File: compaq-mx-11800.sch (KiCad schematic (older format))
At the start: 238 parts

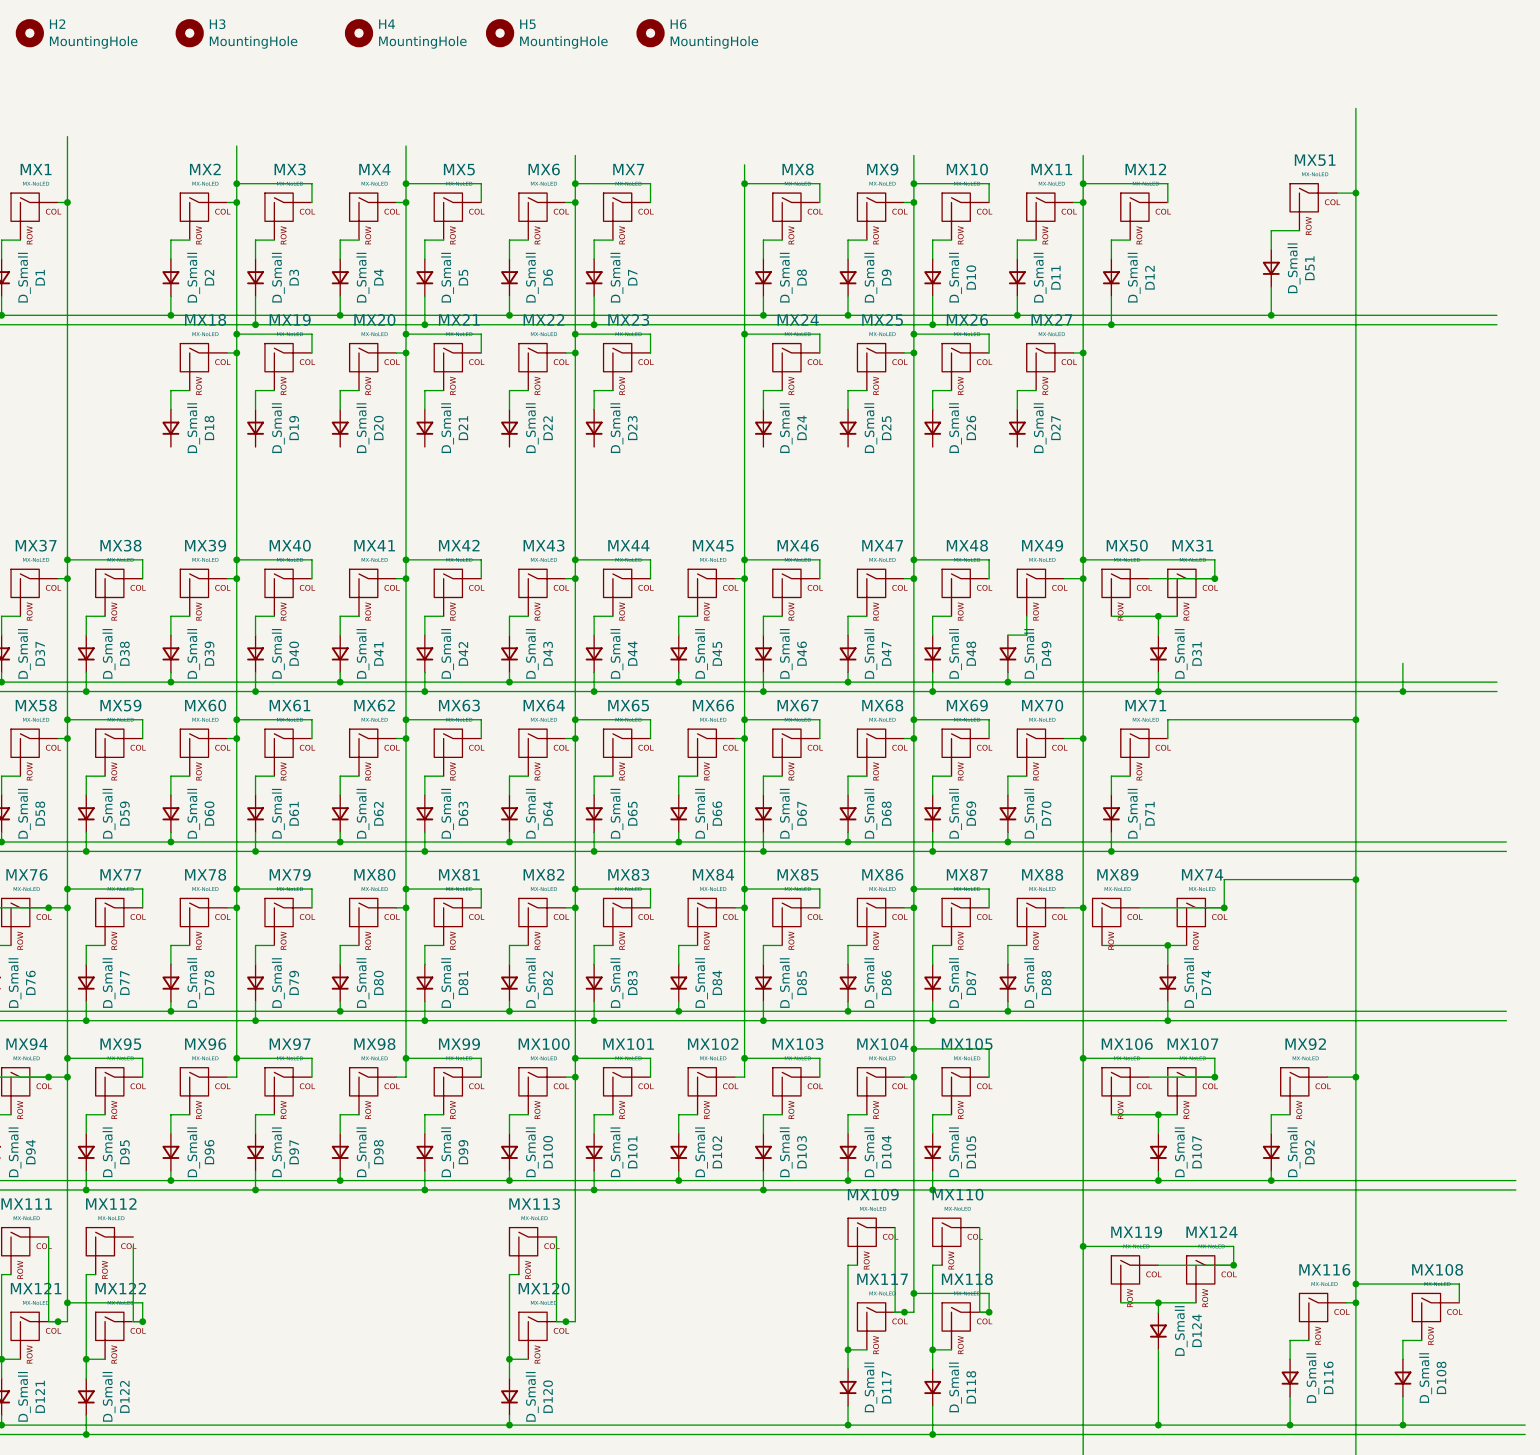
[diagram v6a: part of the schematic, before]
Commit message: fix multilayout column pin connections
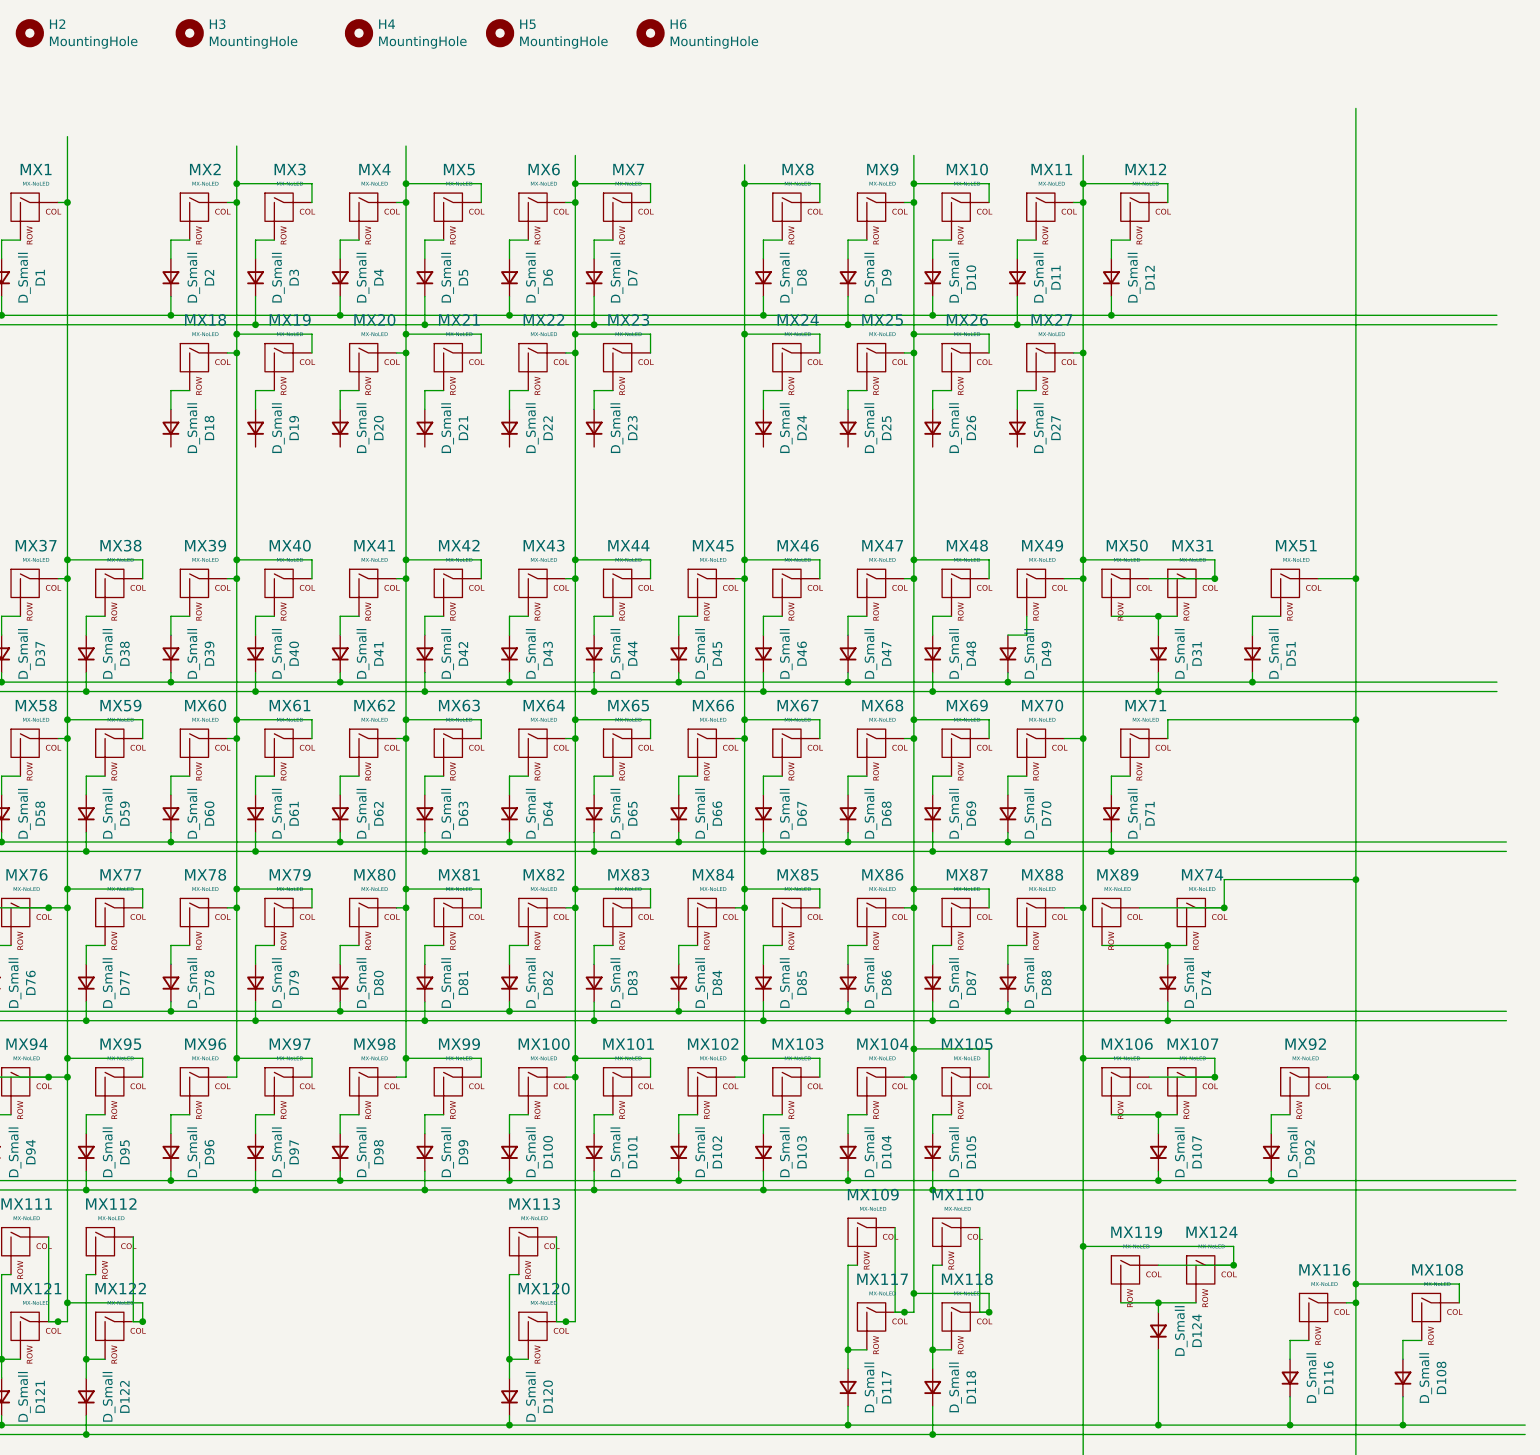
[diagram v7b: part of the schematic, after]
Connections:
- wire segments 748 -> 746
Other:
- moved on the sheet: D51, MX51
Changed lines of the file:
@@
 Wire Wire Line
 	8200 10600 8900 10600
-Wire Wire Line
-	14800 8700 16850 8700
-Connection ~ 14800 8700
-Wire Wire Line
-	14800 8550 14800 8700
-Wire Wire Line
-	14300 8650 15650 8650
-Connection ~ 14300 8650
-Wire Wire Line
-	14300 8550 14300 8650
-Wire Wire Line
-	13400 8650 14300 8650
-Wire Wire Line
-	13850 8700 14800 8700
-Connection ~ 13850 8700
-Wire Wire Line
-	13850 8550 13850 8700
-Connection ~ 13400 8650
-Wire Wire Line
-	13400 8550 13400 8650
-Wire Wire Line
-	12050 8700 13850 8700
-Wire Wire Line
-	12950 8650 13400 8650
 Connection ~ 12950 8650
 Wire Wire Line
-	15650 8650 16850 8650
-Connection ~ 15650 8650
-Wire Wire Line
-	15650 8500 15650 8650
-Wire Wire Line
 	12950 8550 12950 8650
 Connection ~ 12050 8700
@@
 L Device:D_Small D51
 U 1 1 61E61DC5
-P 15650 8400
-F 0 "D51" H 15650 8193 50  0000 C CNN
-F 1 "D_Small" H 15650 8284 50  0000 C CNN
-F 2 "Keebio-Parts:Diode-dual" V 15650 8400 50  0001 C CNN
-F 3 "~" V 15650 8400 50  0001 C CNN
-	1    15650 8400
+P 15550 10450
+F 0 "D51" H 15550 10243 50  0000 C CNN
+F 1 "D_Small" H 15550 10334 50  0000 C CNN
+F 2 "Keebio-Parts:Diode-dual" V 15550 10450 50  0001 C CNN
+F 3 "~" V 15550 10450 50  0001 C CNN
+	1    15550 10450
 	0    -1   -1   0
 $EndComp
@@
 L MX_Alps_Hybrid:MX-NoLED MX51
 U 1 1 61E61DCB
-P 15850 8050
-F 0 "MX51" H 15883 8273 60  0000 C CNN
-F 1 "MX-NoLED" H 15883 8199 20  0000 C CNN
-F 2 "MX_Only:MXOnly-1U-NoLED" H 15225 8025 60  0001 C CNN
-F 3 "" H 15225 8025 60  0001 C CNN
-	1    15850 8050
+P 15750 10100
+F 0 "MX51" H 15783 10323 60  0000 C CNN
+F 1 "MX-NoLED" H 15783 10249 20  0000 C CNN
+F 2 "MX_Only:MXOnly-1U-NoLED" H 15125 10075 60  0001 C CNN
+F 3 "" H 15125 10075 60  0001 C CNN
+	1    15750 10100
 	1    0    0    -1
 $EndComp
 Wire Wire Line
-	15800 8200 15650 8200
-Wire Wire Line
-	15650 8200 15650 8300
-Wire Wire Line
-	16000 8000 16100 8000
-Connection ~ 16100 8000
+	15700 10250 15550 10250
 Wire Wire Line
-	16100 7550 16100 8000
+	15550 10250 15550 10350
 $Comp
 L MX_Alps_Hybrid:MX-NoLED MX1
@@
 Connection ~ 15650 13250
 Wire Wire Line
-	14250 10600 16850 10600
+	14250 10600 15550 10600
 Connection ~ 14650 13600
 Wire Wire Line
@@
 	10050 17250 10050 17350
 Wire Wire Line
-	16350 10650 16850 10650
-Wire Wire Line
-	15050 10650 16350 10650
-Connection ~ 16350 10650
-Wire Wire Line
-	16350 10500 16350 10650
-Wire Wire Line
 	16350 14100 16350 14200
 Wire Wire Line
@@
 Connection ~ 16100 13800
 Wire Wire Line
-	16100 8000 16100 10800
-Wire Wire Line
 	16350 14400 16350 14550
 Wire Wire Line
@@
 Connection ~ 11900 14000
 Wire Wire Line
-	9600 13600 9600 14000
-Wire Wire Line
 	9600 14000 9650 14000
 Connection ~ 9650 14000
@@
 	9150 14000 9200 14000
 Connection ~ 9200 14000
+Wire Wire Line
+	12050 8700 13400 8700
+Wire Wire Line
+	12950 8650 13850 8650
+Wire Wire Line
+	13400 8550 13400 8700
+Connection ~ 13400 8700
+Wire Wire Line
+	13850 8550 13850 8650
+Connection ~ 13850 8650
+Wire Wire Line
+	13850 8650 14800 8650
+Wire Wire Line
+	14300 8550 14300 8700
+Wire Wire Line
+	13400 8700 14300 8700
+Connection ~ 14300 8700
+Wire Wire Line
+	14800 8550 14800 8650
+Connection ~ 14800 8650
+Wire Wire Line
+	14800 8650 16850 8650
+Wire Wire Line
+	16100 7550 16100 10050
+Wire Wire Line
+	15550 10550 15550 10600
+Connection ~ 15550 10600
+Wire Wire Line
+	15550 10600 16850 10600
+Wire Wire Line
+	15900 10050 16100 10050
+Connection ~ 16100 10050
+Wire Wire Line
+	16100 10050 16100 10800
+Wire Wire Line
+	15050 10650 16850 10650
+Wire Wire Line
+	14300 8700 16850 8700
+Wire Wire Line
+	9600 13550 9600 14000
 $EndSCHEMATC

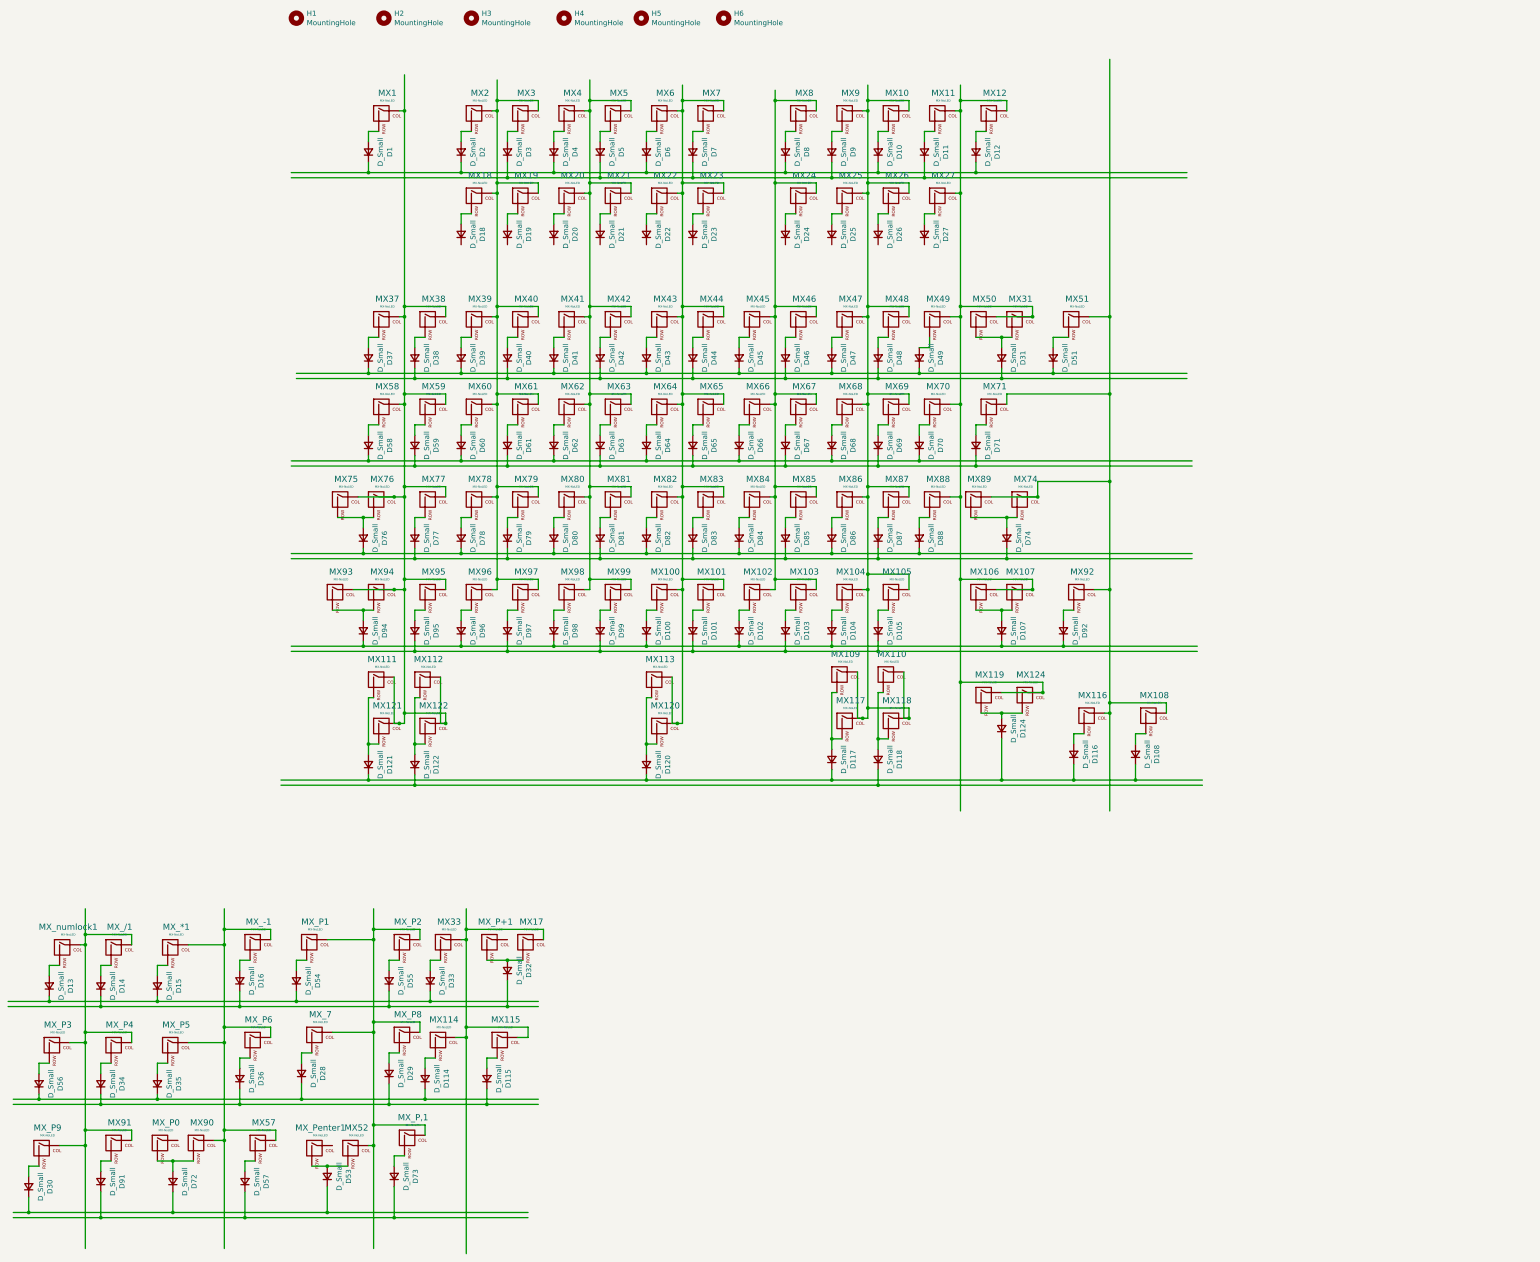
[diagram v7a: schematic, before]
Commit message: connect numpad to existing rows and columns
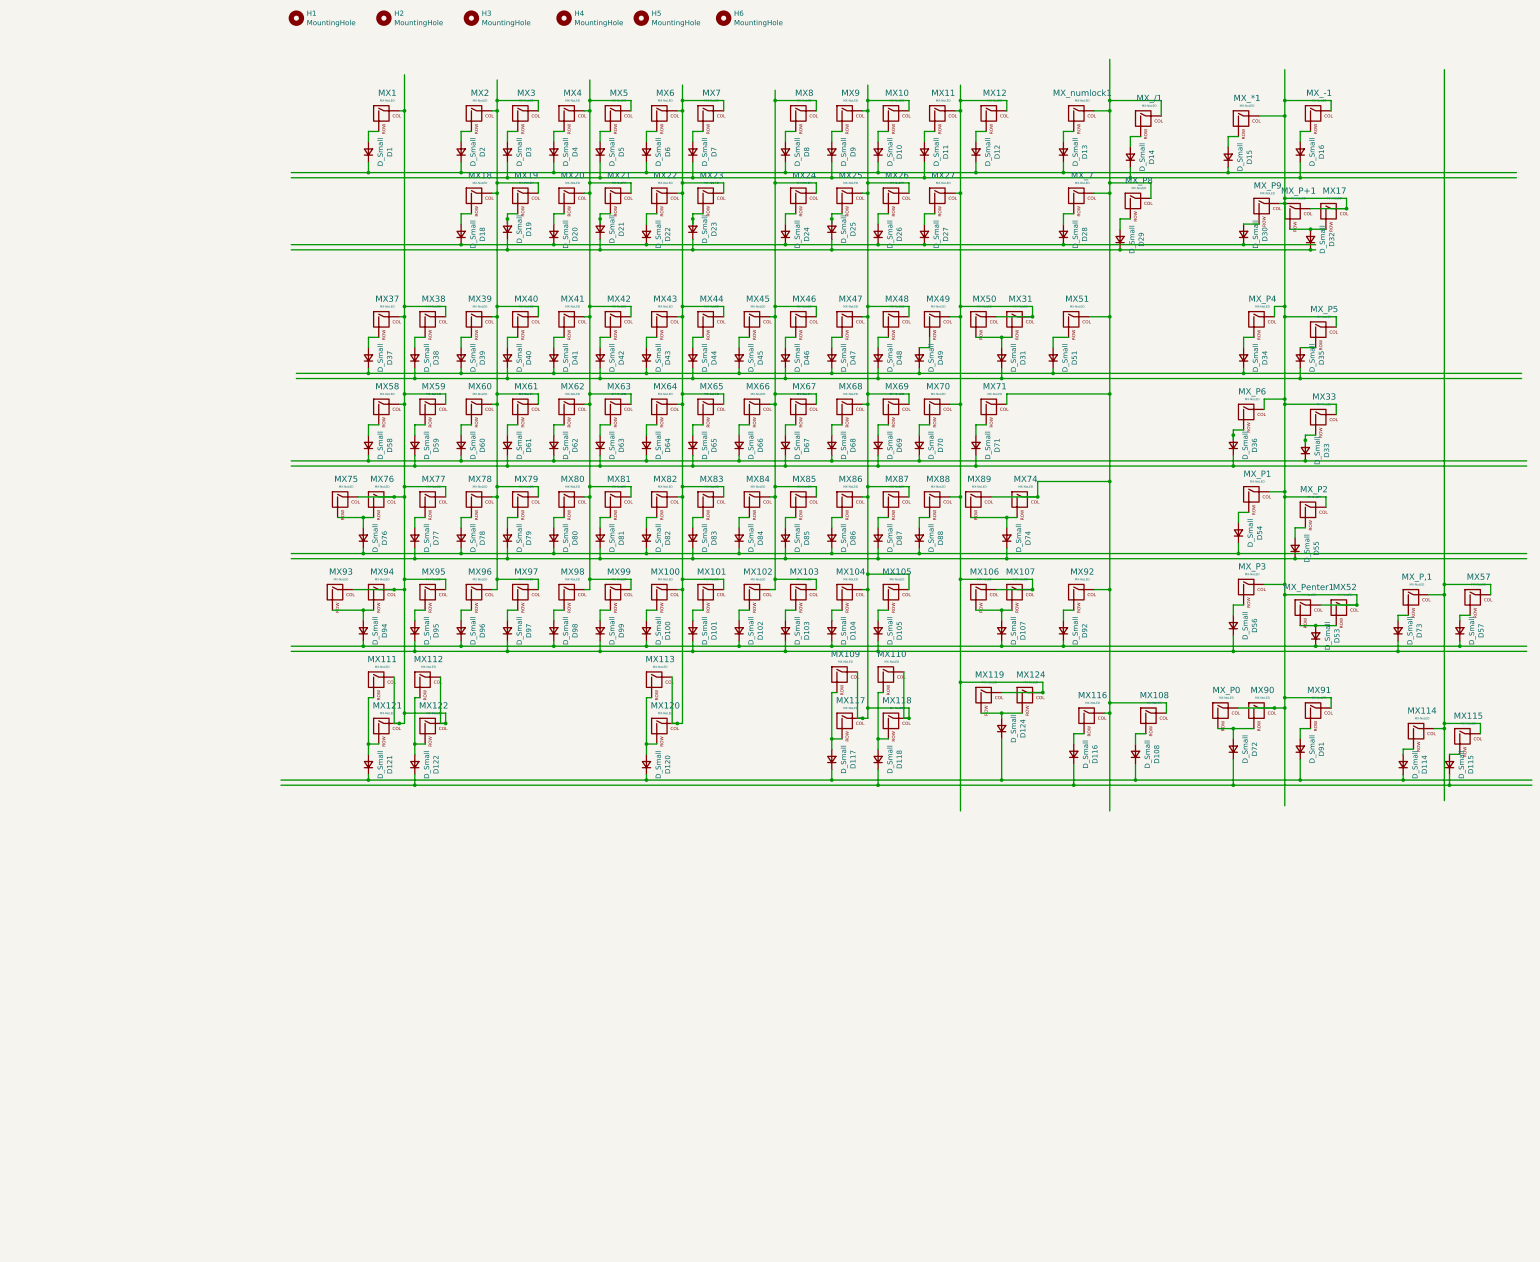
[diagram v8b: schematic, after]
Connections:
- wire segments 746 -> 754
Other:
- moved on the sheet: D114, D115, D13, D14, D15, D16, D19, D21, D23, D25, D28, D29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
